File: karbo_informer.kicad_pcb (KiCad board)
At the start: 2 copper layers, 12 parts, among them IC1 MAX7219, IC2 MAX7219, P1 USB_OTG

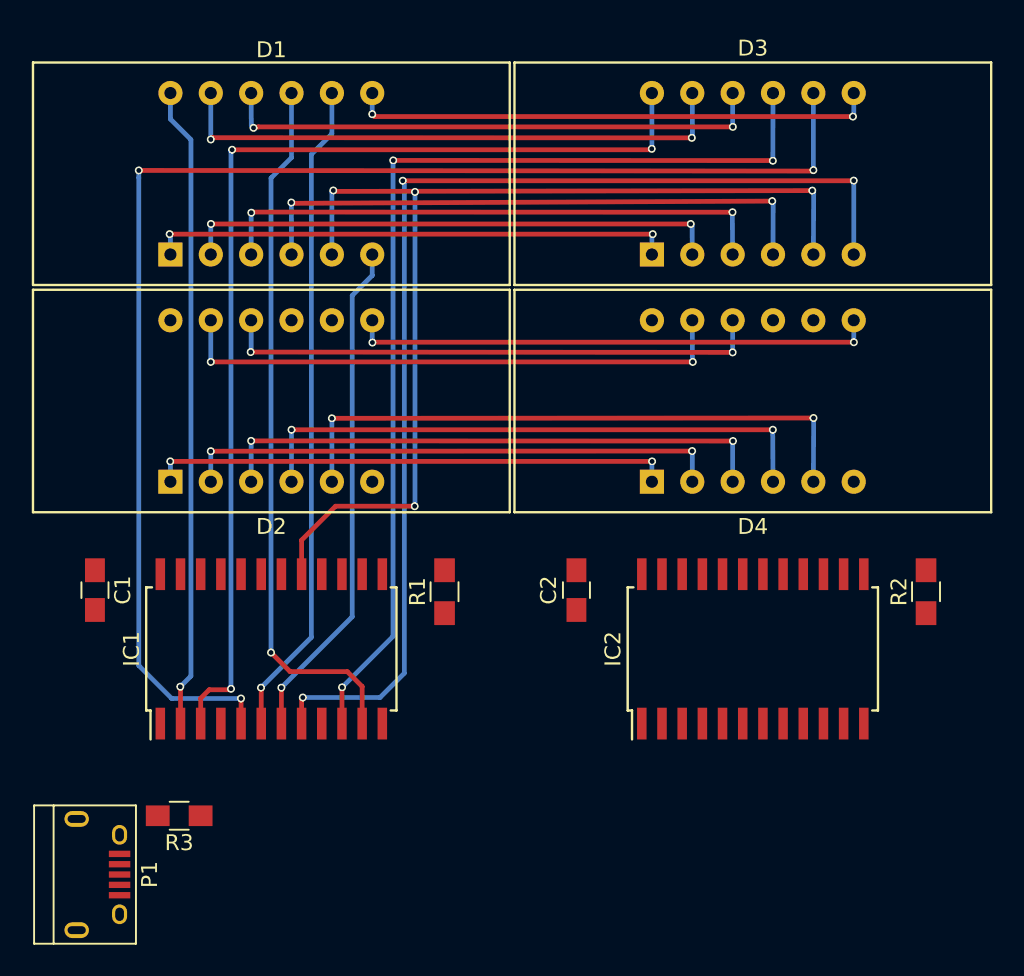
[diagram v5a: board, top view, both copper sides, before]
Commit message: Wire for SEG_B to MAX7219 in the buy line
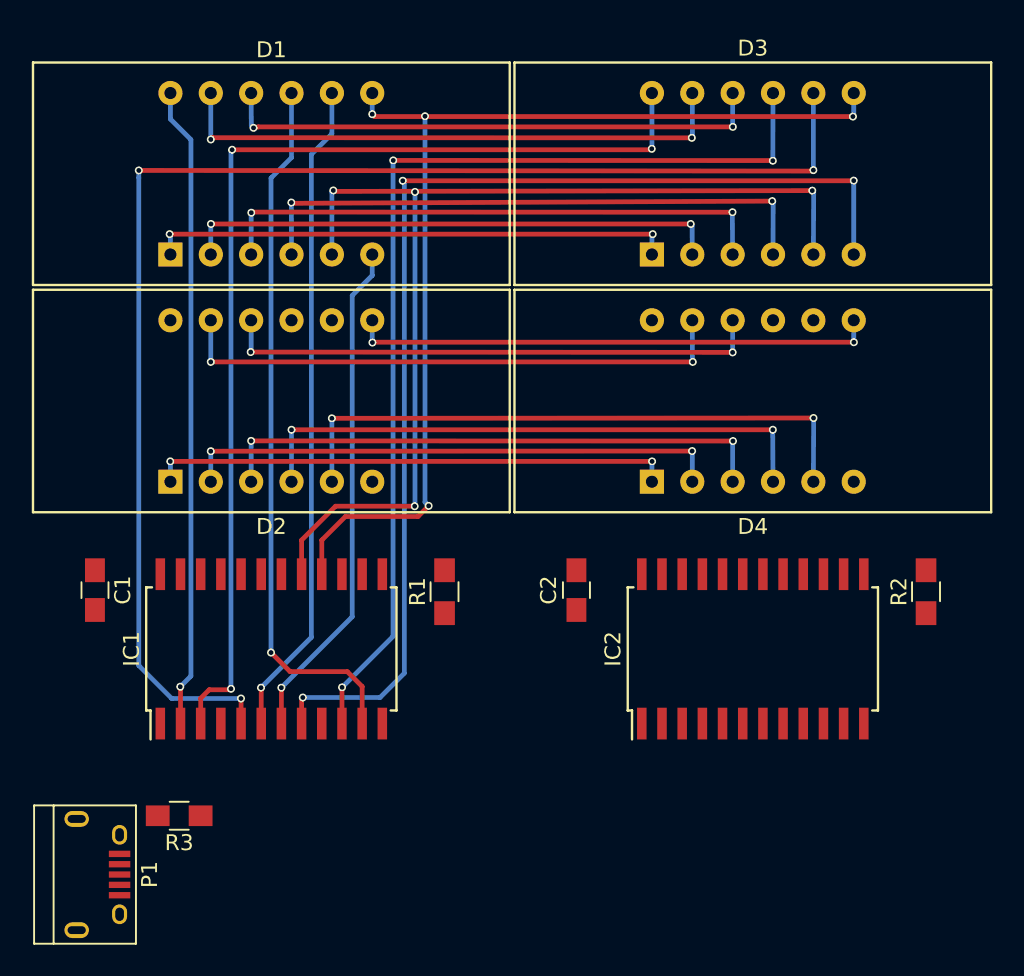
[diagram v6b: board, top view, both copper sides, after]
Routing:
- net /B_SEG_B: track 33.6 -> 68.1 mm, vias 2 -> 4
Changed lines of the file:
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@@
   (general
     (links 69)
-    (no_connects 44)
+    (no_connects 43)
     (area 0 0 0 0)
     (thickness 1.6)
     (drawings 0)
-    (tracks 191)
+    (tracks 203)
     (zones 0)
     (modules 12)
@@
   (via (at 37 32.06) (size 0.5) (drill 0.3) (layers F.Cu B.Cu) (net 3))
   (via (at 42.06 30.71) (size 0.5) (drill 0.3) (layers F.Cu B.Cu) (net 4))
-  (segment (start 72.37 33.98) (end 72.38 30.68) (width 0.3) (layer B.Cu) (net 4) (status 400000))
+  (segment (start 72.37 33.98) (end 72.38 30.68) (width 0.3) (layer B.Cu) (net 4))
   (segment (start 72.32 30.62) (end 72.38 30.68) (width 0.3) (layer B.Cu) (net 4))
   (via (at 72.32 30.62) (size 0.5) (drill 0.3) (layers F.Cu B.Cu) (net 4))
   (segment (start 42.11 30.76) (end 72.32 30.62) (width 0.3) (layer F.Cu) (net 4))
   (segment (start 42.11 30.76) (end 42.06 30.71) (width 0.3) (layer F.Cu) (net 4))
-  (segment (start 42.07 33.98) (end 42.06 30.71) (width 0.3) (layer B.Cu) (net 4) (status 400000))
+  (segment (start 42.07 33.98) (end 42.06 30.71) (width 0.3) (layer B.Cu) (net 4))
   (segment (start 42.06 30.71) (end 42.07 30.7) (width 0.3) (layer B.Cu) (net 4))
+  (segment (start 49.829936 30.029936) (end 49.829936 30.001573) (width 0.3) (layer F.Cu) (net 5))
+  (segment (start 49.84 30.04) (end 49.829936 30.029936) (width 0.3) (layer F.Cu) (net 5))
   (via (at 49.84 30.04) (size 0.5) (drill 0.3) (layers F.Cu B.Cu) (net 5))
+  (segment (start 49.829936 30.001573) (end 74.84 29.96) (width 0.3) (layer F.Cu) (net 5))
   (segment (start 42.705 51.955) (end 44.84 49.82) (width 0.3) (layer F.Cu) (net 5))
   (segment (start 44.84 49.82) (end 49.82 49.82) (width 0.3) (layer F.Cu) (net 5))
@@
   (segment (start 49.82 49.82) (end 49.84 49.8) (width 0.3) (layer B.Cu) (net 5))
   (segment (start 49.84 49.8) (end 49.84 30.04) (width 0.3) (layer B.Cu) (net 5))
-  (segment (start 42.705 54.1) (end 42.705 51.955) (width 0.3) (layer F.Cu) (net 5) (status 400000))
-  (segment (start 49.829936 30.029936) (end 49.829936 30.001573) (width 0.3) (layer F.Cu) (net 5))
-  (segment (start 49.84 30.04) (end 49.829936 30.029936) (width 0.3) (layer F.Cu) (net 5))
-  (segment (start 44.61 33.98) (end 44.61 30.04) (width 0.3) (layer B.Cu) (net 5) (status 400000))
-  (segment (start 74.93 30.05) (end 74.91 33.98) (width 0.3) (layer B.Cu) (net 5) (status 800000))
+  (segment (start 42.705 54.1) (end 42.705 51.955) (width 0.3) (layer F.Cu) (net 5))
+  (segment (start 44.61 33.98) (end 44.61 30.04) (width 0.3) (layer B.Cu) (net 5))
+  (segment (start 74.93 30.05) (end 74.91 33.98) (width 0.3) (layer B.Cu) (net 5))
   (segment (start 74.84 29.96) (end 74.93 30.05) (width 0.3) (layer B.Cu) (net 5))
   (via (at 74.84 29.96) (size 0.5) (drill 0.3) (layers F.Cu B.Cu) (net 5))
   (segment (start 44.76 30.01) (end 49.829936 30.001573) (width 0.3) (layer F.Cu) (net 5))
-  (segment (start 49.829936 30.001573) (end 74.84 29.96) (width 0.3) (layer F.Cu) (net 5))
   (segment (start 44.7 29.95) (end 44.76 30.01) (width 0.3) (layer F.Cu) (net 5))
   (via (at 44.7 29.95) (size 0.5) (drill 0.3) (layers F.Cu B.Cu) (net 5))
@@
   (segment (start 43.32 27.68) (end 43.32 58.07) (width 0.3) (layer B.Cu) (net 11))
   (segment (start 44.61 26.39) (end 43.32 27.68) (width 0.3) (layer B.Cu) (net 11))
+  (segment (start 43.975 54.1) (end 43.975 51.955) (width 0.3) (layer F.Cu) (net 12) (status 400000))
+  (via (at 50.47 25.28) (size 0.5) (drill 0.3) (layers F.Cu B.Cu) (net 12))
+  (segment (start 50.47 49.57) (end 50.47 25.28) (width 0.3) (layer B.Cu) (net 12))
+  (segment (start 50.7 49.8) (end 50.47 49.57) (width 0.3) (layer B.Cu) (net 12))
+  (via (at 50.7 49.8) (size 0.5) (drill 0.3) (layers F.Cu B.Cu) (net 12))
+  (segment (start 50.03 50.47) (end 50.7 49.8) (width 0.3) (layer F.Cu) (net 12))
+  (segment (start 45.46 50.47) (end 50.03 50.47) (width 0.3) (layer F.Cu) (net 12))
+  (segment (start 43.975 51.955) (end 45.46 50.47) (width 0.3) (layer F.Cu) (net 12))
+  (segment (start 50.47 25.28) (end 50.47 25.3) (width 0.3) (layer F.Cu) (net 12))
+  (segment (start 50.47 25.3) (end 50.47 25.28) (width 0.3) (layer F.Cu) (net 12))
+  (segment (start 50.47 25.28) (end 50.47 25.3) (width 0.3) (layer F.Cu) (net 12))
   (via (at 77.4 25.3) (size 0.5) (drill 0.3) (layers F.Cu B.Cu) (net 12))
   (segment (start 77.4 25.3) (end 77.45 25.3) (width 0.3) (layer B.Cu) (net 12))
@@
   (via (at 47.15 25.15) (size 0.5) (drill 0.3) (layers F.Cu B.Cu) (net 12))
   (segment (start 47.15 23.82) (end 47.15 25.15) (width 0.3) (layer B.Cu) (net 12))
-  (segment (start 47.3 25.3) (end 77.4 25.3) (width 0.3) (layer F.Cu) (net 12))
+  (segment (start 47.3 25.3) (end 50.47 25.3) (width 0.3) (layer F.Cu) (net 12))
+  (segment (start 50.47 25.3) (end 77.4 25.3) (width 0.3) (layer F.Cu) (net 12))
   (segment (start 77.4 25.3) (end 77.5 25.3) (width 0.3) (layer F.Cu) (net 12))
   (segment (start 47.15 25.15) (end 47.3 25.3) (width 0.3) (layer F.Cu) (net 12))
@@
   (segment (start 47.18 39.5) (end 77.46 39.5) (width 0.3) (layer F.Cu) (net 24))
   (via (at 47.16 39.52) (size 0.5) (drill 0.3) (layers F.Cu B.Cu) (net 24))
-  (segment (start 74.91 23.82) (end 74.91 28.67) (width 0.3) (layer B.Cu) (net 25) (status 400000))
-  (segment (start 38.895 61.925) (end 38.895 63.5) (width 0.3) (layer F.Cu) (net 25) (status 800000))
+  (segment (start 74.91 23.82) (end 74.91 28.67) (width 0.3) (layer B.Cu) (net 25))
+  (segment (start 38.895 61.925) (end 38.895 63.5) (width 0.3) (layer F.Cu) (net 25))
   (segment (start 38.89 61.92) (end 38.895 61.925) (width 0.3) (layer F.Cu) (net 25))
   (via (at 38.89 61.92) (size 0.5) (drill 0.3) (layers F.Cu B.Cu) (net 25))
@@
   (segment (start 72.34 28.07) (end 48.47 28.06) (width 0.3) (layer F.Cu) (net 27))
   (via (at 72.36 28.08) (size 0.5) (drill 0.3) (layers F.Cu B.Cu) (net 27))
-  (segment (start 45.245 61.225) (end 45.245 63.5) (width 0.3) (layer F.Cu) (net 27) (status 800000))
+  (segment (start 45.245 61.225) (end 45.245 63.5) (width 0.3) (layer F.Cu) (net 27))
   (segment (start 45.25 61.22) (end 45.245 61.225) (width 0.3) (layer F.Cu) (net 27))
   (via (at 45.25 61.22) (size 0.5) (drill 0.3) (layers F.Cu B.Cu) (net 27))
@@
   (segment (start 48.46 28.07) (end 48.46 58.01) (width 0.3) (layer B.Cu) (net 27))
   (segment (start 48.47 28.06) (end 48.46 28.07) (width 0.3) (layer B.Cu) (net 27))
-  (segment (start 72.37 23.82) (end 72.36 28.08) (width 0.3) (layer B.Cu) (net 27) (status 400000))
-  (segment (start 77.45 33.98) (end 77.45 29.33) (width 0.3) (layer B.Cu) (net 33) (status 400000))
-  (segment (start 42.705 61.935) (end 42.705 63.5) (width 0.3) (layer F.Cu) (net 33) (status 800000))
+  (segment (start 72.37 23.82) (end 72.36 28.08) (width 0.3) (layer B.Cu) (net 27))
+  (segment (start 77.45 33.98) (end 77.45 29.33) (width 0.3) (layer B.Cu) (net 33))
+  (segment (start 42.705 61.935) (end 42.705 63.5) (width 0.3) (layer F.Cu) (net 33))
   (segment (start 42.78 61.86) (end 42.705 61.935) (width 0.3) (layer F.Cu) (net 33))
   (via (at 42.78 61.86) (size 0.5) (drill 0.3) (layers F.Cu B.Cu) (net 33))
